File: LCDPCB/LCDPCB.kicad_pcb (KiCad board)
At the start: 2 copper layers, 60 x 64 mm, 32 parts, among them J1 Sockets, J2 Hot Plug, J3 Programming Header, J4 Conn_01x08_Male, J5 Conn_01x08_Male, SW1 SW_Push, U1 STM32F091RCT6, U2 LD1117S12TR_SOT223

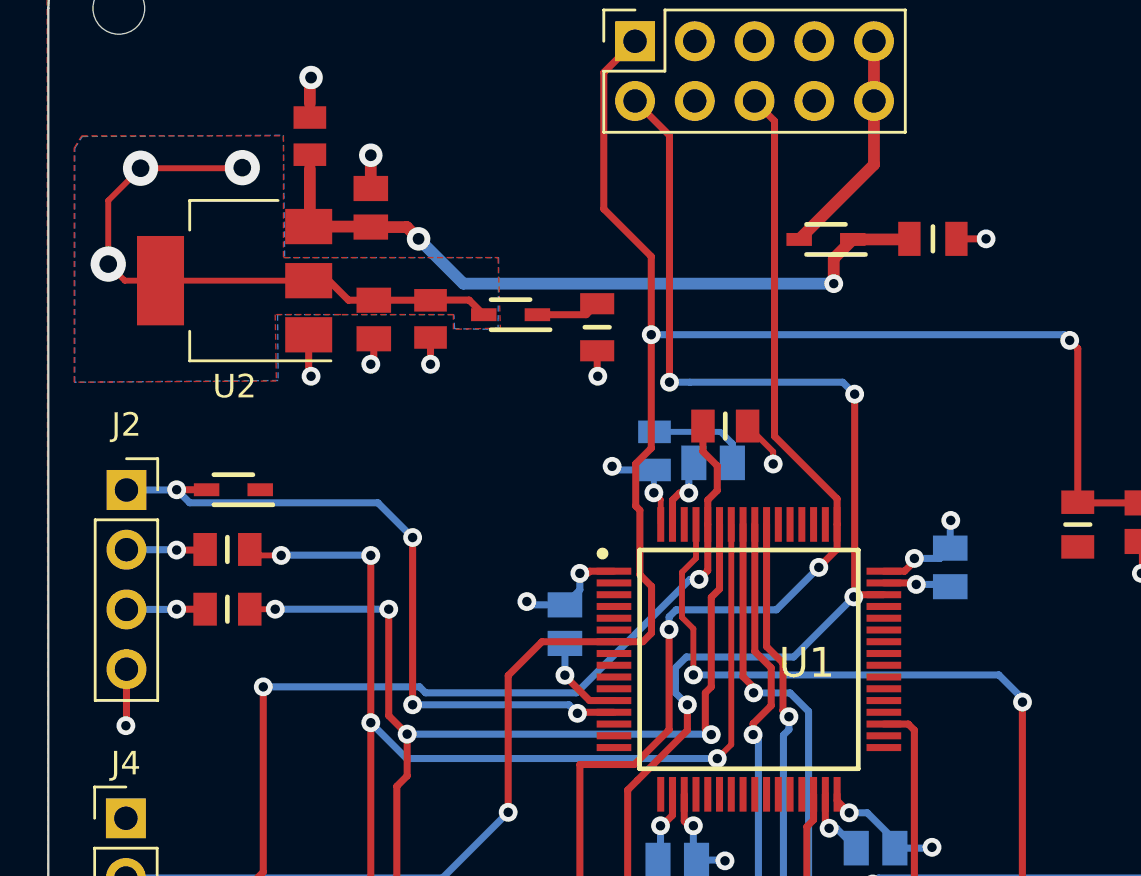
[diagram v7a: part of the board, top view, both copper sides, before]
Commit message: minor cosmetic change
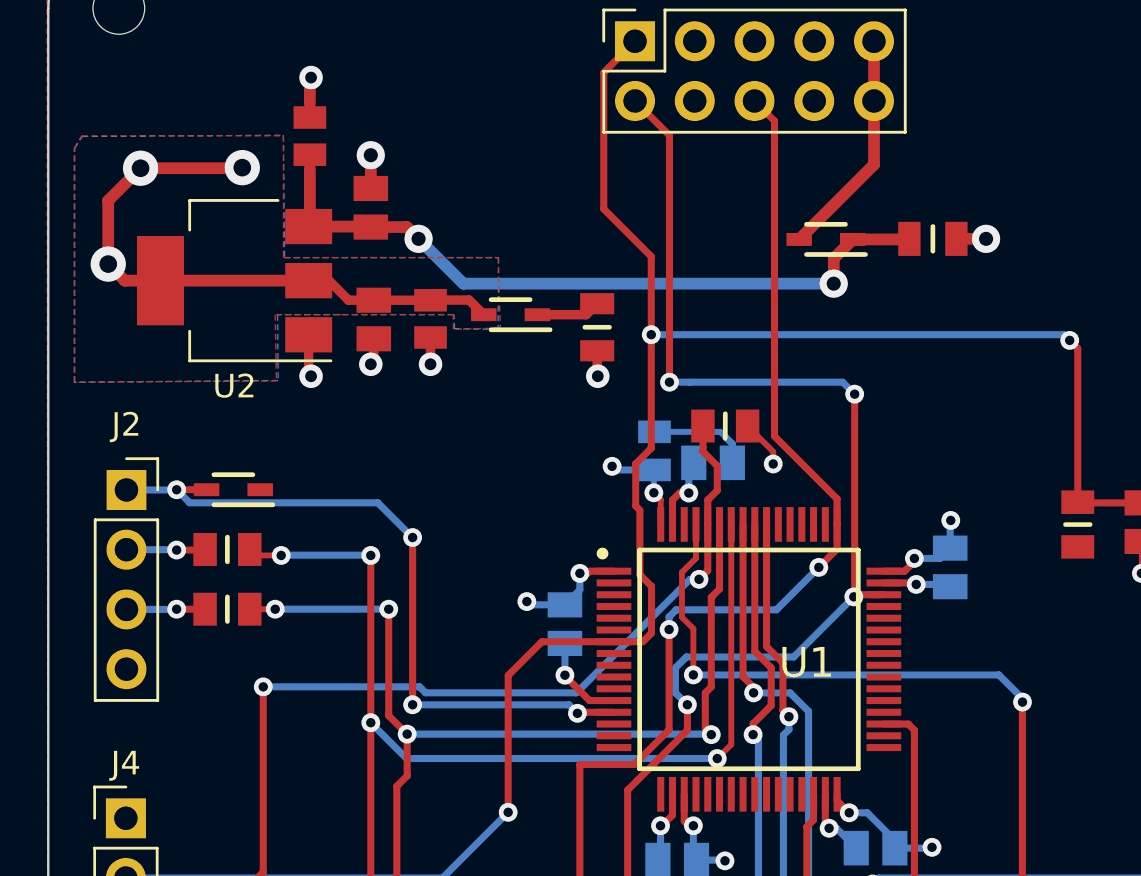
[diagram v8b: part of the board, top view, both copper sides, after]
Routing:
- net GND: track 32.5 -> 30.1 mm, vias 16 -> 15
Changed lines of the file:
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@@
   (segment (start 130.556 91.186) (end 127.762 93.98) (width 0.3) (layer "B.Cu") (net 1))
   (segment (start 154.19 70.878) (end 154.432 71.12) (width 0.3) (layer "B.Cu") (net 1))
-  (segment (start 114.325 87.478) (end 114.3 87.503) (width 0.3) (layer "F.Cu") (net 2))
   (segment (start 157.5 81.006) (end 157.48 81.026) (width 0.25) (layer "F.Cu") (net 2))
   (segment (start 134.3406 72.6186) (end 134.366 72.644) (width 0.3) (layer "F.Cu") (net 2))
   (segment (start 122.1232 59.9948) (end 122.174 59.944) (width 0.5) (layer "F.Cu") (net 2))
-  (segment (start 127.254 71.0056) (end 127.254 72.136) (width 0.3) (layer "F.Cu") (net 2))
+  (segment (start 127.254 71.0056) (end 127.254 72.136) (width 0.4) (layer "F.Cu") (net 2))
   (segment (start 138.236323 77.610225) (end 137.840075 77.610225) (width 0.3) (layer "F.Cu") (net 2))
-  (segment (start 149.6154 66.802) (end 150.876 66.802) (width 0.3) (layer "F.Cu") (net 2))
+  (segment (start 149.6154 66.802) (end 150.876 66.802) (width 0.5) (layer "F.Cu") (net 2))
   (segment (start 137.840075 77.610225) (end 137.5422 77.9081) (width 0.3) (layer "F.Cu") (net 2))
   (segment (start 124.841 72.009) (end 124.714 72.136) (width 0.3) (layer "F.Cu") (net 2))
@@
   (segment (start 137.033 91.758602) (end 137.095398 91.758602) (width 0.3) (layer "F.Cu") (net 2))
   (segment (start 141.825 75.851) (end 140.737 74.763) (width 0.25) (layer "F.Cu") (net 2))
-  (segment (start 114.325 85.1) (end 114.325 87.478) (width 0.3) (layer "F.Cu") (net 2))
   (segment (start 144.0422 91.704154) (end 144.0422 90.4216) (width 0.3) (layer "F.Cu") (net 2))
   (segment (start 146.5302 81.4336) (end 147.84363 81.4336) (width 0.3) (layer "F.Cu") (net 2))
   (segment (start 157.5 79.67) (end 157.5 81.006) (width 0.25) (layer "F.Cu") (net 2))
   (segment (start 137.5422 91.3118) (end 137.5422 90.4216) (width 0.3) (layer "F.Cu") (net 2))
-  (segment (start 124.841 71.051) (end 124.841 72.009) (width 0.3) (layer "F.Cu") (net 2))
+  (segment (start 124.841 71.051) (end 124.841 72.009) (width 0.4) (layer "F.Cu") (net 2))
   (segment (start 132.969 85.3859) (end 134.0167 86.4336) (width 0.3) (layer "F.Cu") (net 2))
   (segment (start 160.0052 84.3568) (end 161.5152 84.3568) (width 0.3) (layer "F.Cu") (net 2))
@@
   (segment (start 137.5422 77.9081) (end 137.5422 78.9456) (width 0.3) (layer "F.Cu") (net 2))
   (segment (start 124.714 64.6612) (end 124.714 63.246) (width 0.5) (layer "F.Cu") (net 2))
-  (segment (start 134.3406 71.5612) (end 134.3406 72.6186) (width 0.3) (layer "F.Cu") (net 2))
+  (segment (start 134.3406 71.5612) (end 134.3406 72.6186) (width 0.4) (layer "F.Cu") (net 2))
   (segment (start 122.0728 72.5428) (end 122.174 72.644) (width 0.3) (layer "F.Cu") (net 2))
-  (segment (start 122.0728 70.88) (end 122.0728 72.5428) (width 0.3) (layer "F.Cu") (net 2))
-  (via (at 127.254 72.136) (size 0.8) (drill 0.4) (layers "F.Cu" "B.Cu") (net 2))
+  (segment (start 122.0728 70.88) (end 122.0728 72.5428) (width 0.4) (layer "F.Cu") (net 2))
+  (via (at 127.254 72.136) (size 1) (drill 0.5) (layers "F.Cu" "B.Cu") (net 2))
   (via (at 122.174 59.944) (size 1) (drill 0.5) (layers "F.Cu" "B.Cu") (net 2))
-  (via (at 134.366 72.644) (size 0.8) (drill 0.4) (layers "F.Cu" "B.Cu") (net 2))
+  (via (at 134.366 72.644) (size 1) (drill 0.5) (layers "F.Cu" "B.Cu") (net 2))
   (via (at 147.906875 81.496845) (size 0.8) (drill 0.4) (layers "F.Cu" "B.Cu") (net 2))
   (via (at 144.202243 91.864197) (size 0.8) (drill 0.4) (layers "F.Cu" "B.Cu") (net 2))
   (via (at 161.544 84.328) (size 0.8) (drill 0.4) (layers "F.Cu" "B.Cu") (net 2))
-  (via (at 124.714 63.246) (size 1) (drill 0.5) (layers "F.Cu" "B.Cu") (net 2))
+  (via (at 124.714 63.246) (size 1.2) (drill 0.6) (layers "F.Cu" "B.Cu") (net 2))
   (via (at 141.825 76.375) (size 0.8) (drill 0.4) (layers "F.Cu" "B.Cu") (net 2))
-  (via (at 150.876 66.802) (size 0.8) (drill 0.4) (layers "F.Cu" "B.Cu") (net 2))
-  (via (at 114.3 87.503) (size 0.8) (drill 0.4) (layers "F.Cu" "B.Cu") (net 2))
+  (via (at 150.876 66.802) (size 1.2) (drill 0.6) (layers "F.Cu" "B.Cu") (net 2))
   (via (at 138.236323 77.610225) (size 0.8) (drill 0.4) (layers "F.Cu" "B.Cu") (net 2))
   (via (at 137.033 91.758602) (size 0.8) (drill 0.4) (layers "F.Cu" "B.Cu") (net 2))
-  (via (at 122.174 72.644) (size 0.8) (drill 0.4) (layers "F.Cu" "B.Cu") (net 2))
+  (via (at 122.174 72.644) (size 1) (drill 0.5) (layers "F.Cu" "B.Cu") (net 2))
   (via (at 157.48 81.026) (size 0.8) (drill 0.4) (layers "F.Cu" "B.Cu") (net 2))
   (via (at 132.969 85.3565) (size 0.8) (drill 0.4) (layers "F.Cu" "B.Cu") (net 2))
-  (via (at 124.714 72.136) (size 0.8) (drill 0.4) (layers "F.Cu" "B.Cu") (net 2))
+  (via (at 124.714 72.136) (size 1) (drill 0.5) (layers "F.Cu" "B.Cu") (net 2))
   (segment (start 137.033 91.758602) (end 137.033 93.1092) (width 0.3) (layer "B.Cu") (net 2))
   (segment (start 147.906875 81.496845) (end 149.256845 81.496845) (width 0.3) (layer "B.Cu") (net 2))
@@
   (segment (start 138.240602 91.758602) (end 138.0422 91.5602) (width 0.3) (layer "F.Cu") (net 3))
   (segment (start 133.9243 81.026) (end 134.0167 80.9336) (width 0.3) (layer "F.Cu") (net 3))
-  (segment (start 131.7976 70.0278) (end 133.874 70.0278) (width 0.3) (layer "F.Cu") (net 3))
+  (segment (start 131.7976 70.0278) (end 133.874 70.0278) (width 0.4) (layer "F.Cu") (net 3))
   (segment (start 147.4124 80.9336) (end 146.5302 80.9336) (width 0.3) (layer "F.Cu") (net 3))
-  (segment (start 133.874 70.0278) (end 134.3406 69.5612) (width 0.3) (layer "F.Cu") (net 3))
+  (segment (start 133.874 70.0278) (end 134.3406 69.5612) (width 0.4) (layer "F.Cu") (net 3))
   (segment (start 137.0422 78.9456) (end 137.0422 77.8922) (width 0.25) (layer "F.Cu") (net 3))
   (segment (start 145.057558 91.207003) (end 144.5422 90.691645) (width 0.3) (layer "F.Cu") (net 3))
@@
   (segment (start 124.6928 66.28) (end 124.714 66.3012) (width 0.5) (layer "F.Cu") (net 4))
   (segment (start 145.2088 66.8274) (end 144.399 67.6372) (width 0.5) (layer "F.Cu") (net 4))
-  (via (at 126.746 66.802) (size 1) (drill 0.5) (layers "F.Cu" "B.Cu") (net 4))
-  (via (at 144.399 68.707) (size 0.8) (drill 0.4) (layers "F.Cu" "B.Cu") (net 4))
+  (via (at 126.746 66.802) (size 1.2) (drill 0.6) (layers "F.Cu" "B.Cu") (net 4))
+  (via (at 144.399 68.707) (size 1.2) (drill 0.6) (layers "F.Cu" "B.Cu") (net 4))
   (segment (start 144.399 68.707) (end 128.651 68.707) (width 0.5) (layer "B.Cu") (net 4))
   (segment (start 128.651 68.707) (end 126.746 66.802) (width 0.5) (layer "B.Cu") (net 4))
@@
   (segment (start 116.459 82.55) (end 116.449 82.56) (width 0.3) (layer "B.Cu") (net 69))
   (segment (start 116.449 82.56) (end 114.325 82.56) (width 0.3) (layer "B.Cu") (net 69))
-  (segment (start 128.8954 69.4056) (end 129.5176 70.0278) (width 0.3) (layer "F.Cu") (net 70))
-  (segment (start 114.925 63.8) (end 119.225 63.8) (width 0.25) (layer "F.Cu") (net 70))
-  (segment (start 124.841 69.411) (end 127.2486 69.411) (width 0.3) (layer "F.Cu") (net 70))
+  (segment (start 128.8954 69.4056) (end 129.5176 70.0278) (width 0.4) (layer "F.Cu") (net 70))
+  (segment (start 114.925 63.8) (end 119.225 63.8) (width 0.5) (layer "F.Cu") (net 70))
+  (segment (start 124.841 69.411) (end 127.2486 69.411) (width 0.4) (layer "F.Cu") (net 70))
   (segment (start 119.225 63.8) (end 119.25 63.775) (width 0.25) (layer "F.Cu") (net 70))
-  (segment (start 115.7728 68.58) (end 114.255 68.58) (width 0.25) (layer "F.Cu") (net 70))
-  (segment (start 114.255 68.58) (end 113.55 67.875) (width 0.25) (layer "F.Cu") (net 70))
-  (segment (start 127.254 69.4056) (end 128.8954 69.4056) (width 0.3) (layer "F.Cu") (net 70))
-  (segment (start 123.767 69.411) (end 124.841 69.411) (width 0.3) (layer "F.Cu") (net 70))
-  (segment (start 122.0728 68.58) (end 115.7728 68.58) (width 0.25) (layer "F.Cu") (net 70))
+  (segment (start 115.7728 68.58) (end 114.255 68.58) (width 0.5) (layer "F.Cu") (net 70))
+  (segment (start 114.255 68.58) (end 113.55 67.875) (width 0.5) (layer "F.Cu") (net 70))
+  (segment (start 127.254 69.4056) (end 128.8954 69.4056) (width 0.4) (layer "F.Cu") (net 70))
+  (segment (start 123.767 69.411) (end 124.841 69.411) (width 0.4) (layer "F.Cu") (net 70))
+  (segment (start 122.0728 68.58) (end 115.7728 68.58) (width 0.5) (layer "F.Cu") (net 70))
   (segment (start 127.2486 69.411) (end 127.254 69.4056) (width 0.3) (layer "F.Cu") (net 70))
   (segment (start 122.0728 68.58) (end 122.936 68.58) (width 0.25) (layer "F.Cu") (net 70))
-  (segment (start 113.55 65.175) (end 114.925 63.8) (width 0.25) (layer "F.Cu") (net 70))
-  (segment (start 113.55 67.875) (end 113.55 65.175) (width 0.25) (layer "F.Cu") (net 70))
-  (segment (start 122.936 68.58) (end 123.767 69.411) (width 0.3) (layer "F.Cu") (net 70))
+  (segment (start 113.55 65.175) (end 114.925 63.8) (width 0.5) (layer "F.Cu") (net 70))
+  (segment (start 113.55 67.875) (end 113.55 65.175) (width 0.5) (layer "F.Cu") (net 70))
+  (segment (start 122.936 68.58) (end 123.767 69.411) (width 0.4) (layer "F.Cu") (net 70))
   (via (at 113.55 67.875) (size 1.5) (drill 0.75) (layers "F.Cu" "B.Cu") (free) (net 70))
   (via (at 114.925 63.8) (size 1.5) (drill 0.75) (layers "F.Cu" "B.Cu") (free) (net 70))
